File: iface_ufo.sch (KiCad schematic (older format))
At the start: 2 parts, among them J6000 CW308_TARGETCON, J6200 CW_PWR

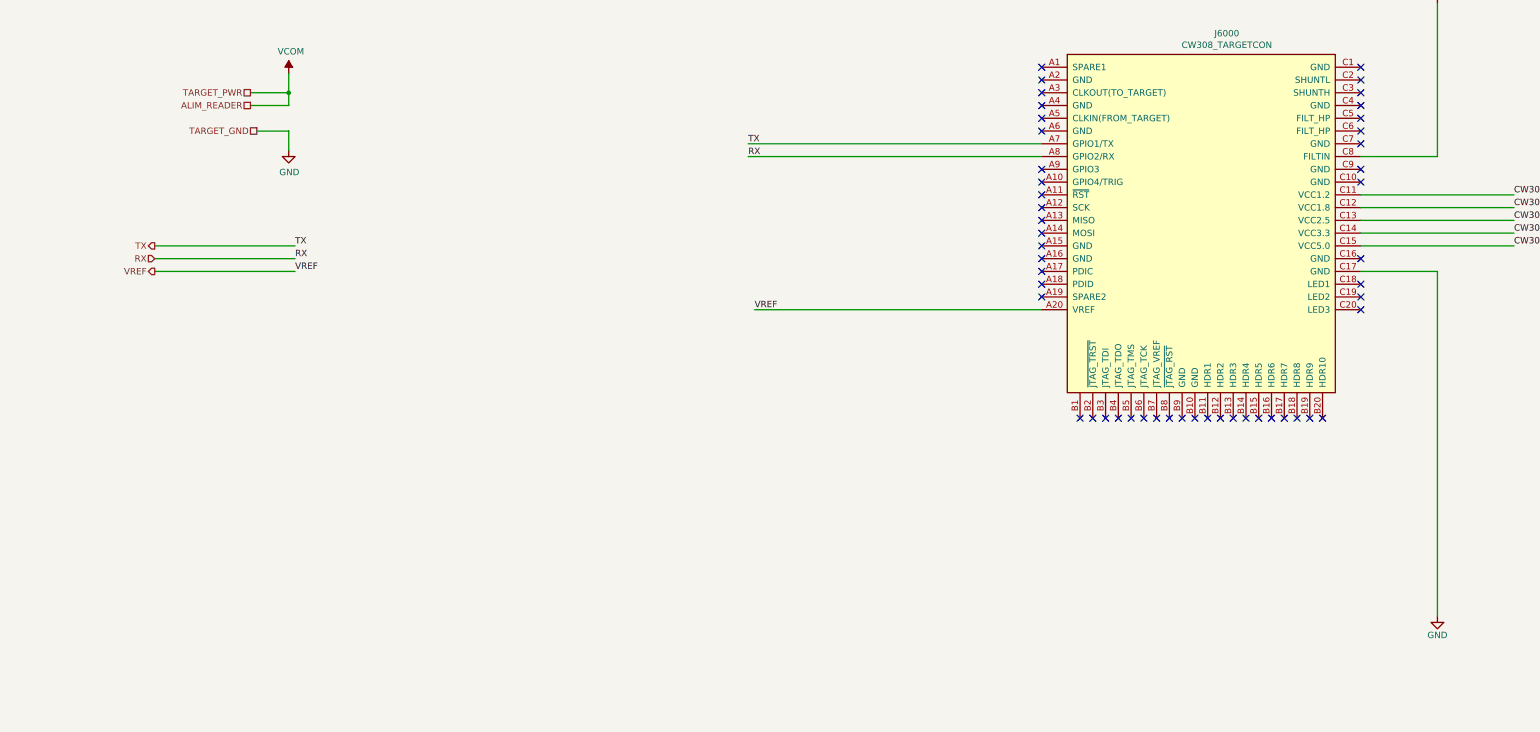
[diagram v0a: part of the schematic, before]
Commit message: [enhancement] Add tests points for smartcard controlled triggers, connect PB4 to CARD_CLK for bitbanging mode
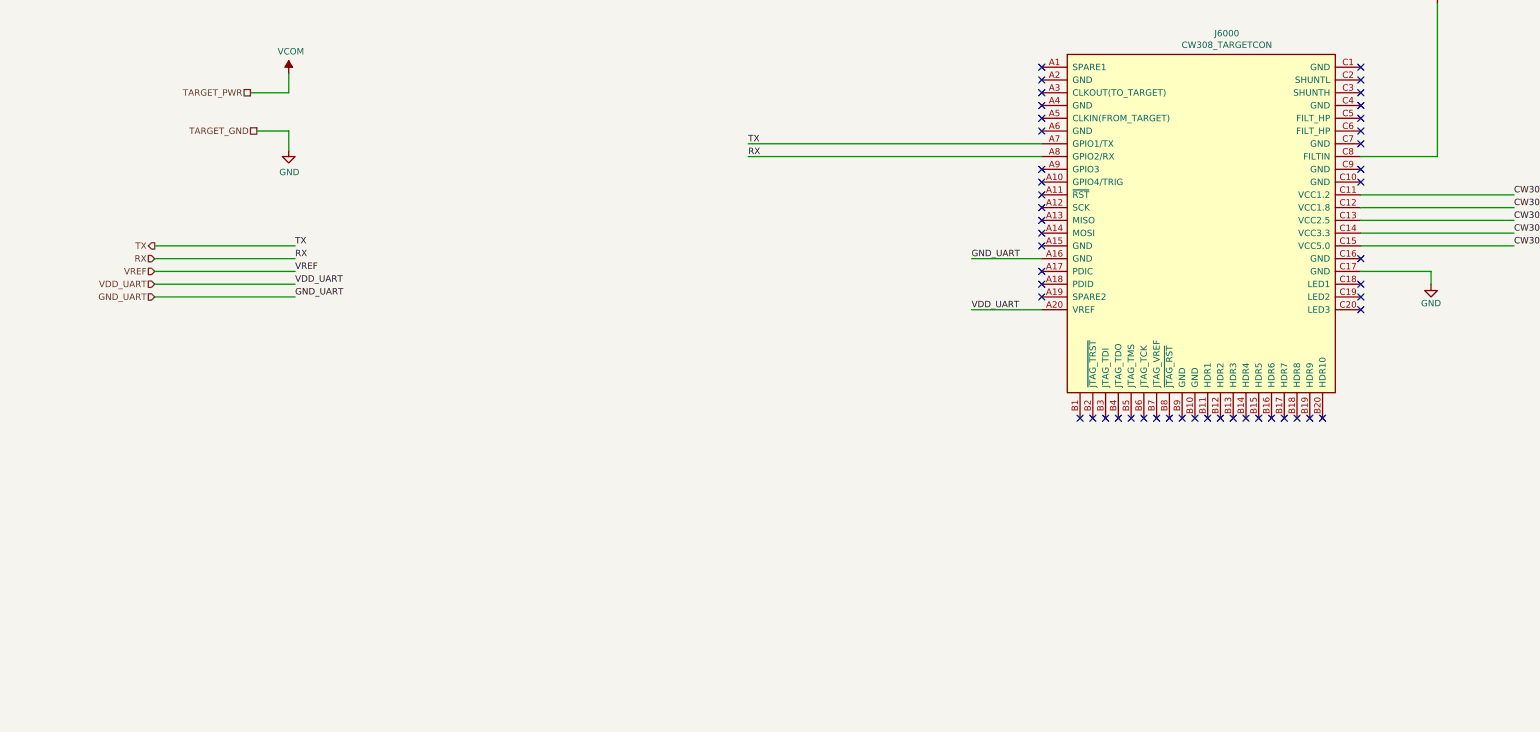
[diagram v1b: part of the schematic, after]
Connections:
- net VREF: no longer J6000.A20 (VREF)
- net GND_UART: now reaches J6000.A16 (GND)
- new net VDD_UART: J6000.A20 (VREF)
- no-connect marks 51 -> 50
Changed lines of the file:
@@
 Text HLabel 3650 7500 0    50   Output ~ 0
 TX
-Text HLabel 4400 6400 0    50   UnSpc ~ 0
-ALIM_READER
 Wire Wire Line
 	3650 7600 4750 7600
@@
 CW308_5.0
 Wire Wire Line
-	10600 8000 8350 8000
+	10600 8000 10050 8000
 NoConn ~ 12300 8850
 NoConn ~ 12400 8850
@@
 Wire Wire Line
 	4450 6600 4700 6600
-$Comp
-L leia-rescue:GND #PWR0122
-U 1 1 5C4D696F
-P 13700 10400
-F 0 "#PWR0122" H 13700 10150 50  0001 C CNN
-F 1 "GND" H 13700 10250 50  0000 C CNN
-F 2 "" H 13700 10400 60  0000 C CNN
-F 3 "" H 13700 10400 60  0000 C CNN
-	1    13700 10400
-	1    0    0    -1
-$EndComp
 Wire Wire Line
 	11700 5150 11100 5150
@@
 	1    0    0    -1
 $EndComp
-Wire Wire Line
-	13700 7700 13700 10400
 NoConn ~ 11700 8850
 NoConn ~ 11800 8850
 NoConn ~ 12000 8850
 NoConn ~ 12200 8850
-NoConn ~ 10600 7600
 NoConn ~ 10600 7500
 NoConn ~ 10600 6400
@@
 Wire Wire Line
 	13100 7400 14300 7400
-Wire Wire Line
-	13100 7700 13700 7700
 $Comp
 L wisp:CW308_TARGETCON J6000
@@
 NoConn ~ 11700 5350
 Wire Wire Line
-	4400 6400 4700 6400
-Wire Wire Line
 	10600 6700 8300 6700
 Wire Wire Line
@@
 Text Label 8300 6800 0    50   ~ 0
 RX
-Text Label 8350 8000 0    50   ~ 0
-VREF
 Text Label 4750 7700 0    50   ~ 0
 VREF
-Text HLabel 3650 7700 0    50   Output ~ 0
+Text HLabel 3650 7700 0    50   Input ~ 0
 VREF
 Wire Wire Line
@@
 Wire Wire Line
 	13050 4000 13050 4850
-Wire Wire Line
-	4700 6400 4700 6300
-Connection ~ 4700 6300
 Wire Wire Line
 	4700 6300 4700 6150
@@
 NoConn ~ 13100 6300
 NoConn ~ 10900 8850
+Wire Wire Line
+	10600 7600 10050 7600
+$Comp
+L leia-rescue:GND #PWR0118
+U 1 1 5D03631E
+P 13650 7800
+F 0 "#PWR0118" H 13650 7550 50  0001 C CNN
+F 1 "GND" H 13650 7650 50  0000 C CNN
+F 2 "" H 13650 7800 60  0000 C CNN
+F 3 "" H 13650 7800 60  0000 C CNN
+	1    13650 7800
+	1    0    0    -1
+$EndComp
+Wire Wire Line
+	3650 7800 4750 7800
+Text Label 4750 7800 0    50   ~ 0
+VDD_UART
+Wire Wire Line
+	13100 7700 13650 7700
+Wire Wire Line
+	13650 7700 13650 7800
+Text HLabel 3650 7800 0    50   Input ~ 0
+VDD_UART
+Text HLabel 3650 7900 0    50   Input ~ 0
+GND_UART
+Text Label 4750 7900 0    50   ~ 0
+GND_UART
+Wire Wire Line
+	3650 7900 4750 7900
+Text Label 10050 7600 0    50   ~ 0
+GND_UART
+Text Label 10050 8000 0    50   ~ 0
+VDD_UART
 $EndSCHEMATC

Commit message: [enhancement] WIP working on power domain isolation
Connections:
- net VDD_UART is gone; now on net VREF: J6000.A20 (VREF)
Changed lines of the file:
@@
 Text Label 14300 7500 0    50   ~ 0
 CW308_5.0
-Wire Wire Line
-	10600 8000 10050 8000
 NoConn ~ 12300 8850
 NoConn ~ 12400 8850
@@
 $EndComp
 Wire Wire Line
-	3650 7800 4750 7800
-Text Label 4750 7800 0    50   ~ 0
-VDD_UART
-Wire Wire Line
 	13100 7700 13650 7700
 Wire Wire Line
 	13650 7700 13650 7800
-Text HLabel 3650 7800 0    50   Input ~ 0
-VDD_UART
 Text HLabel 3650 7900 0    50   Input ~ 0
 GND_UART
@@
 Wire Wire Line
 	3650 7900 4750 7900
+Text Label 10050 8000 0    50   ~ 0
+VREF
+Wire Wire Line
+	10600 8000 10050 8000
 Text Label 10050 7600 0    50   ~ 0
 GND_UART
-Text Label 10050 8000 0    50   ~ 0
-VDD_UART
 $EndSCHEMATC

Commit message: [enhancement] Rework cw308 trigger con.
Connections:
- net GND_UART is gone; now on net GND: J6000.A16 (GND)
- net GND: now also J6000.C4 (GND); no longer J6000.C17 (GND)
- net VCOM: no longer J6000.C8 (FILTIN)
- net VREF: now also J6000.C8 (FILTIN)
- net CW_TRIG: now reaches J6000.A10 (GPIO4/TRIG)
- no-connect marks 50 -> 49
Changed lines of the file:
@@
 	13100 7100 14300 7100
-$Comp
-L power:VCOM #PWR0124
-U 1 1 5C6F8DB8
-P 13700 5600
-F 0 "#PWR0124" H 13700 5450 50  0001 C CNN
-F 1 "VCOM" H 13717 5773 50  0000 C CNN
-F 2 "" H 13700 5600 50  0001 C CNN
-F 3 "" H 13700 5600 50  0001 C CNN
-	1    13700 5600
-	1    0    0    -1
-$EndComp
 $Comp
 L power:VCOM #PWR0125
@@
 NoConn ~ 10600 6400
 NoConn ~ 10600 6200
-NoConn ~ 13100 6400
 NoConn ~ 13100 6500
 NoConn ~ 13100 6600
@@
 	1    0    0    -1
 $EndComp
-Wire Wire Line
-	13700 6800 13700 5600
-Wire Wire Line
-	13100 6800 13700 6800
 Text HLabel 4400 6300 0    50   UnSpc ~ 0
 TARGET_PWR
@@
 NoConn ~ 10600 7300
 NoConn ~ 10600 7400
-NoConn ~ 10600 7000
 NoConn ~ 11300 8850
 NoConn ~ 11400 8850
@@
 L leia-rescue:GND #PWR0118
 U 1 1 5D03631E
-P 13650 7800
-F 0 "#PWR0118" H 13650 7550 50  0001 C CNN
-F 1 "GND" H 13650 7650 50  0000 C CNN
-F 2 "" H 13650 7800 60  0000 C CNN
-F 3 "" H 13650 7800 60  0000 C CNN
-	1    13650 7800
-	1    0    0    -1
-$EndComp
-Wire Wire Line
-	13100 7700 13650 7700
-Wire Wire Line
-	13650 7700 13650 7800
-Text HLabel 3650 7900 0    50   Input ~ 0
-GND_UART
-Text Label 4750 7900 0    50   ~ 0
-GND_UART
-Wire Wire Line
-	3650 7900 4750 7900
+P 13650 6500
+F 0 "#PWR0118" H 13650 6250 50  0001 C CNN
+F 1 "GND" H 13650 6350 50  0000 C CNN
+F 2 "" H 13650 6500 60  0000 C CNN
+F 3 "" H 13650 6500 60  0000 C CNN
+	1    13650 6500
+	1    0    0    -1
+$EndComp
+Wire Wire Line
+	13100 6400 13650 6400
+Wire Wire Line
+	13650 6400 13650 6500
 Text Label 10050 8000 0    50   ~ 0
 VREF
 Wire Wire Line
 	10600 8000 10050 8000
-Text Label 10050 7600 0    50   ~ 0
-GND_UART
+Wire Wire Line
+	10600 7000 8300 7000
+Text Label 8300 7000 0    50   ~ 0
+CW_TRIG
+Text Label 4750 7400 0    50   ~ 0
+CW_TRIG
+Wire Wire Line
+	4750 7400 3650 7400
+Text HLabel 3650 7400 0    50   Input ~ 0
+CW_TRIG
+Text Label 14300 6800 0    50   ~ 0
+VREF
+Wire Wire Line
+	13100 6800 14300 6800
+$Comp
+L power:GND #PWR0124
+U 1 1 5D414A28
+P 10050 7600
+F 0 "#PWR0124" H 10050 7350 50  0001 C CNN
+F 1 "GND" H 10055 7427 50  0000 C CNN
+F 2 "" H 10050 7600 50  0001 C CNN
+F 3 "" H 10050 7600 50  0001 C CNN
+	1    10050 7600
+	1    0    0    -1
+$EndComp
+NoConn ~ 13100 7700
 $EndSCHEMATC

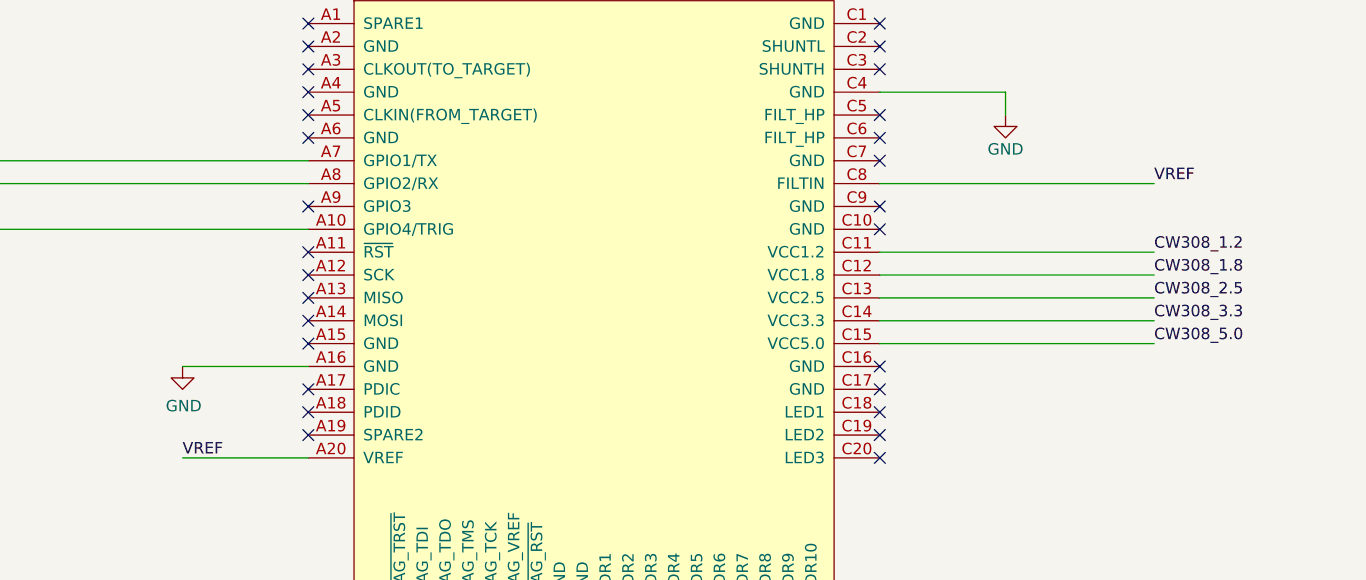
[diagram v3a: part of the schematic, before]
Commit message: [enhancement] Rework Power plan.
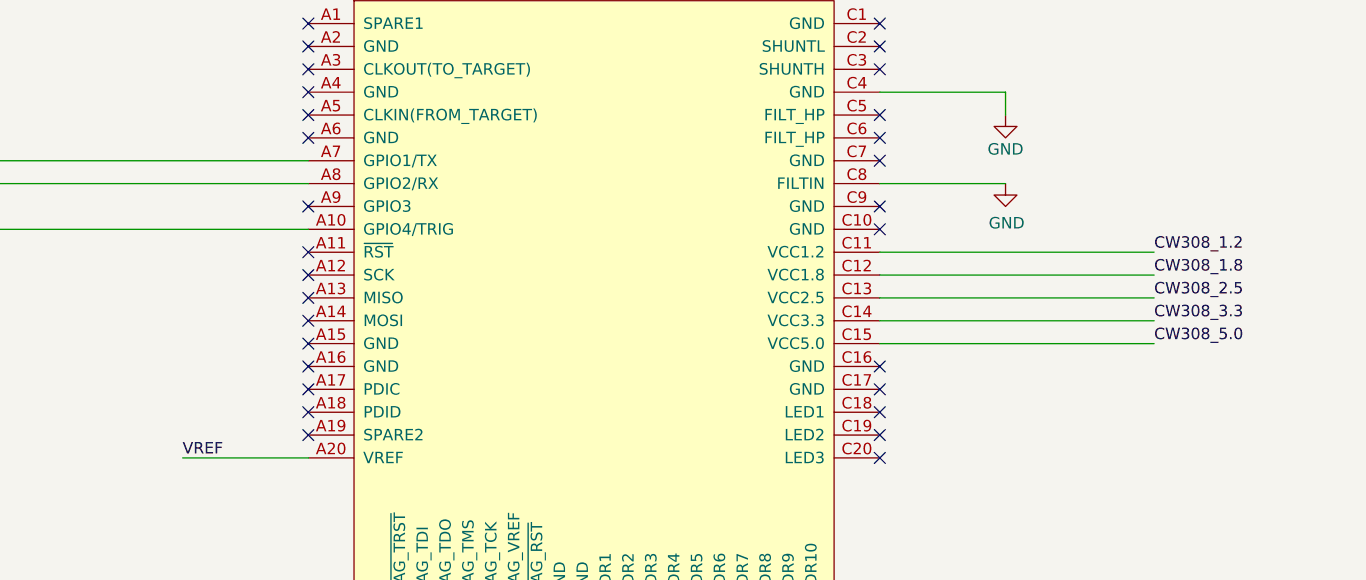
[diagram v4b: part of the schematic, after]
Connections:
- net GND: now also J6000.C8 (FILTIN); no longer J6000.A16 (GND)
- net VREF: no longer J6000.C8 (FILTIN)
- no-connect marks 49 -> 50
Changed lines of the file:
@@
 EESchema Schematic File Version 4
 LIBS:leia-cache
+LIBS:wookey-cache
 EELAYER 29 0
 EELAYER END
 $Descr A2 23386 16535
 encoding utf-8
-Sheet 4 5
+Sheet 5 5
 Title "CW-LEIA"
 Date "2016-28-20"
@@
 NoConn ~ 13100 6300
 NoConn ~ 10900 8850
-Wire Wire Line
-	10600 7600 10050 7600
 $Comp
 L leia-rescue:GND #PWR0118
@@
 Text HLabel 3650 7400 0    50   Input ~ 0
 CW_TRIG
-Text Label 14300 6800 0    50   ~ 0
-VREF
-Wire Wire Line
-	13100 6800 14300 6800
-$Comp
-L power:GND #PWR0124
-U 1 1 5D414A28
-P 10050 7600
-F 0 "#PWR0124" H 10050 7350 50  0001 C CNN
-F 1 "GND" H 10055 7427 50  0000 C CNN
-F 2 "" H 10050 7600 50  0001 C CNN
-F 3 "" H 10050 7600 50  0001 C CNN
-	1    10050 7600
-	1    0    0    -1
-$EndComp
 NoConn ~ 13100 7700
+$Comp
+L power:GND #PWR0122
+U 1 1 5D0B3DF2
+P 13650 6800
+F 0 "#PWR0122" H 13650 6550 50  0001 C CNN
+F 1 "GND" H 13655 6627 50  0000 C CNN
+F 2 "" H 13650 6800 50  0001 C CNN
+F 3 "" H 13650 6800 50  0001 C CNN
+	1    13650 6800
+	1    0    0    -1
+$EndComp
+Wire Wire Line
+	13100 6800 13650 6800
+NoConn ~ 10600 7600
 $EndSCHEMATC

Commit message: [Fix] General cleanup before production
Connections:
- net GND: now also J6000.A16 (GND)
- no-connect marks 50 -> 49
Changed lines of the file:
@@
 Wire Wire Line
 	13100 6800 13650 6800
-NoConn ~ 10600 7600
+Wire Wire Line
+	10600 7600 10050 7600
+$Comp
+L power:GND #PWR0154
+U 1 1 5D44EF88
+P 10050 7600
+F 0 "#PWR0154" H 10050 7350 50  0001 C CNN
+F 1 "GND" H 10055 7427 50  0000 C CNN
+F 2 "" H 10050 7600 50  0001 C CNN
+F 3 "" H 10050 7600 50  0001 C CNN
+	1    10050 7600
+	1    0    0    -1
+$EndComp
 $EndSCHEMATC

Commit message: [fix] ground plans => ready for review
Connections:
- net GND renamed TARGET_GND
